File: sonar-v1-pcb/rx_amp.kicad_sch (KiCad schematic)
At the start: 13 parts, among them U301 Opamp_Dual

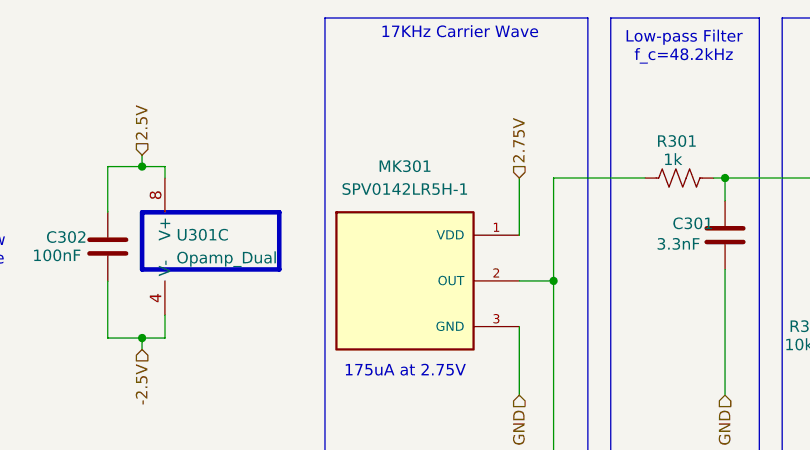
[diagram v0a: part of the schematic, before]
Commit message: Fix pinout
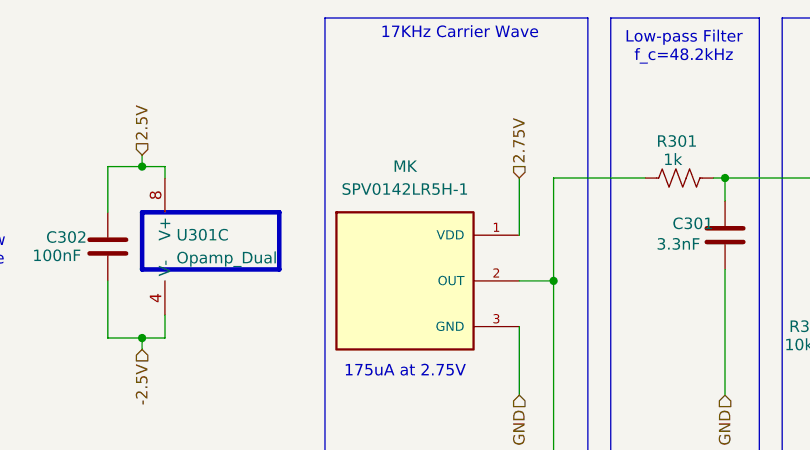
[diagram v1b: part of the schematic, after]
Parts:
- renumbered MK301 to MK

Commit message: Fix the annoattion thing
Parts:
- renumbered MK to MK301
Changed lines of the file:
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@@
 	)
 	(rectangle
-		(start 71.12 80.01)
-		(end 86.36 86.36)
-		(stroke
-			(width 0.508)
-			(type default)
-			(color 255 0 255 1)
-		)
-		(fill
-			(type none)
-		)
-	)
-	(rectangle
 		(start 142.24 58.42)
 		(end 179.07 113.03)
@@
 		)
 	)
-	(rectangle
-		(start 190.5 64.77)
-		(end 205.74 71.12)
-		(stroke
-			(width 0.508)
-			(type default)
-			(color 255 0 255 1)
-		)
-		(fill
-			(type none)
-		)
-	)
-	(rectangle
-		(start 147.32 66.04)
-		(end 162.56 72.39)
-		(stroke
-			(width 0.508)
-			(type default)
-			(color 255 0 255 1)
-		)
-		(fill
-			(type none)
-		)
-	)
 	(text "175uA at 2.75V"
 		(exclude_from_sim no)
@@
 		(dnp no)
 		(fields_autoplaced yes)
-		(property "Reference" "MK"
+		(property "Reference" "MK301"
 			(at 100.33 74.93 0)
 			(effects
@@
 				)
 				(path "/f72ceae0-eee4-4385-b0e8-639846bcb5f2/293969c4-9575-41aa-bb6a-e94ffb52e407/4baae0c7-5504-4fa5-b170-826798e08abe"
-					(reference "MK2102")
+					(reference "MK2101")
 					(unit 1)
 				)
@@
 					(unit 1)
 				)
+				(path "/f72ceae0-eee4-4385-b0e8-639846bcb5f2/d78844ef-eb5d-4b24-a5c3-8824db20c2bc/1e9737bb-54d3-46c6-89c7-bafd5d01cb9f"
+					(reference "MK2601")
+					(unit 1)
+				)
+				(path "/f72ceae0-eee4-4385-b0e8-639846bcb5f2/d78844ef-eb5d-4b24-a5c3-8824db20c2bc/4b88e5a9-a1a4-4236-ac8a-a515268f9e7e"
+					(reference "MK701")
+					(unit 1)
+				)
+				(path "/f72ceae0-eee4-4385-b0e8-639846bcb5f2/d78844ef-eb5d-4b24-a5c3-8824db20c2bc/4baae0c7-5504-4fa5-b170-826798e08abe"
+					(reference "MK301")
+					(unit 1)
+				)
+				(path "/f72ceae0-eee4-4385-b0e8-639846bcb5f2/d78844ef-eb5d-4b24-a5c3-8824db20c2bc/5fa345fd-8f82-4102-b4da-88393397ee2f"
+					(reference "MK1801")
+					(unit 1)
+				)
+				(path "/f72ceae0-eee4-4385-b0e8-639846bcb5f2/d78844ef-eb5d-4b24-a5c3-8824db20c2bc/92589eb0-14ab-438f-abf4-d7e391dbea95"
+					(reference "MK601")
+					(unit 1)
+				)
+				(path "/f72ceae0-eee4-4385-b0e8-639846bcb5f2/d78844ef-eb5d-4b24-a5c3-8824db20c2bc/a69a1e19-7333-49c9-8cfe-abe95e31b9e6"
+					(reference "MK1401")
+					(unit 1)
+				)
+				(path "/f72ceae0-eee4-4385-b0e8-639846bcb5f2/d78844ef-eb5d-4b24-a5c3-8824db20c2bc/da58af52-59a2-42c6-b6e7-fabe3f18277b"
+					(reference "MK1001")
+					(unit 1)
+				)
+				(path "/f72ceae0-eee4-4385-b0e8-639846bcb5f2/d78844ef-eb5d-4b24-a5c3-8824db20c2bc/ef24f3d1-799c-40c0-a32b-fd2185333268"
+					(reference "MK2201")
+					(unit 1)
+				)
 			)
 		)
@@
 				)
 				(path "/f72ceae0-eee4-4385-b0e8-639846bcb5f2/293969c4-9575-41aa-bb6a-e94ffb52e407/5fa345fd-8f82-4102-b4da-88393397ee2f"
-					(reference "U2502")
+					(reference "U2501")
 					(unit 1)
 				)
 				(path "/f72ceae0-eee4-4385-b0e8-639846bcb5f2/293969c4-9575-41aa-bb6a-e94ffb52e407/92589eb0-14ab-438f-abf4-d7e391dbea95"
-					(reference "U2002")
+					(reference "U2001")
 					(unit 1)
 				)
@@
 				)
 				(path "/f72ceae0-eee4-4385-b0e8-639846bcb5f2/d3b8d639-c387-46bd-9010-317ff5495a13/5fa345fd-8f82-4102-b4da-88393397ee2f"
-					(reference "U1303")
+					(reference "U1301")
 					(unit 1)
 				)
 				(path "/f72ceae0-eee4-4385-b0e8-639846bcb5f2/d3b8d639-c387-46bd-9010-317ff5495a13/92589eb0-14ab-438f-abf4-d7e391dbea95"
-					(reference "U802")
+					(reference "U801")
 					(unit 1)
 				)
@@
 			(project "sonar"
 				(path "/f72ceae0-eee4-4385-b0e8-639846bcb5f2/293969c4-9575-41aa-bb6a-e94ffb52e407/1e9737bb-54d3-46c6-89c7-bafd5d01cb9f"
-					(reference "U2502")
+					(reference "U2701")
 					(unit 3)
 				)
@@
 				)
 				(path "/f72ceae0-eee4-4385-b0e8-639846bcb5f2/293969c4-9575-41aa-bb6a-e94ffb52e407/da58af52-59a2-42c6-b6e7-fabe3f18277b"
-					(reference "U2002")
+					(reference "U2301")
 					(unit 3)
 				)
@@
 				)
 				(path "/f72ceae0-eee4-4385-b0e8-639846bcb5f2/d3b8d639-c387-46bd-9010-317ff5495a13/1e9737bb-54d3-46c6-89c7-bafd5d01cb9f"
-					(reference "U1303")
+					(reference "U1501")
 					(unit 3)
 				)
@@
 				)
 				(path "/f72ceae0-eee4-4385-b0e8-639846bcb5f2/d3b8d639-c387-46bd-9010-317ff5495a13/5fa345fd-8f82-4102-b4da-88393397ee2f"
-					(reference "U1302")
+					(reference "U1301")
 					(unit 3)
 				)
@@
 				)
 				(path "/f72ceae0-eee4-4385-b0e8-639846bcb5f2/d3b8d639-c387-46bd-9010-317ff5495a13/a69a1e19-7333-49c9-8cfe-abe95e31b9e6"
-					(reference "U503")
+					(reference "U501")
 					(unit 3)
 				)
 				(path "/f72ceae0-eee4-4385-b0e8-639846bcb5f2/d3b8d639-c387-46bd-9010-317ff5495a13/da58af52-59a2-42c6-b6e7-fabe3f18277b"
-					(reference "U802")
+					(reference "U1101")
 					(unit 3)
 				)
@@
 				)
 				(path "/f72ceae0-eee4-4385-b0e8-639846bcb5f2/d78844ef-eb5d-4b24-a5c3-8824db20c2bc/1e9737bb-54d3-46c6-89c7-bafd5d01cb9f"
-					(reference "U1801")
+					(reference "U2601")
 					(unit 3)
 				)
 				(path "/f72ceae0-eee4-4385-b0e8-639846bcb5f2/d78844ef-eb5d-4b24-a5c3-8824db20c2bc/4b88e5a9-a1a4-4236-ac8a-a515268f9e7e"
-					(reference "U502")
+					(reference "U701")
 					(unit 3)
 				)
@@
 				)
 				(path "/f72ceae0-eee4-4385-b0e8-639846bcb5f2/d78844ef-eb5d-4b24-a5c3-8824db20c2bc/5fa345fd-8f82-4102-b4da-88393397ee2f"
-					(reference "U1101")
+					(reference "U1801")
 					(unit 3)
 				)
 				(path "/f72ceae0-eee4-4385-b0e8-639846bcb5f2/d78844ef-eb5d-4b24-a5c3-8824db20c2bc/92589eb0-14ab-438f-abf4-d7e391dbea95"
-					(reference "U501")
+					(reference "U601")
 					(unit 3)
 				)
 				(path "/f72ceae0-eee4-4385-b0e8-639846bcb5f2/d78844ef-eb5d-4b24-a5c3-8824db20c2bc/a69a1e19-7333-49c9-8cfe-abe95e31b9e6"
-					(reference "U803")
+					(reference "U1401")
 					(unit 3)
 				)
 				(path "/f72ceae0-eee4-4385-b0e8-639846bcb5f2/d78844ef-eb5d-4b24-a5c3-8824db20c2bc/da58af52-59a2-42c6-b6e7-fabe3f18277b"
-					(reference "U601")
+					(reference "U1001")
 					(unit 3)
 				)
 				(path "/f72ceae0-eee4-4385-b0e8-639846bcb5f2/d78844ef-eb5d-4b24-a5c3-8824db20c2bc/ef24f3d1-799c-40c0-a32b-fd2185333268"
-					(reference "U1301")
+					(reference "U2201")
 					(unit 3)
 				)
@@
 			(project "sonar"
 				(path "/f72ceae0-eee4-4385-b0e8-639846bcb5f2/293969c4-9575-41aa-bb6a-e94ffb52e407/1e9737bb-54d3-46c6-89c7-bafd5d01cb9f"
-					(reference "U2502")
+					(reference "U2701")
 					(unit 2)
 				)
@@
 				)
 				(path "/f72ceae0-eee4-4385-b0e8-639846bcb5f2/293969c4-9575-41aa-bb6a-e94ffb52e407/da58af52-59a2-42c6-b6e7-fabe3f18277b"
-					(reference "U2002")
+					(reference "U2301")
 					(unit 2)
 				)
@@
 				)
 				(path "/f72ceae0-eee4-4385-b0e8-639846bcb5f2/d3b8d639-c387-46bd-9010-317ff5495a13/1e9737bb-54d3-46c6-89c7-bafd5d01cb9f"
-					(reference "U1303")
+					(reference "U1501")
 					(unit 2)
 				)
@@
 				)
 				(path "/f72ceae0-eee4-4385-b0e8-639846bcb5f2/d3b8d639-c387-46bd-9010-317ff5495a13/5fa345fd-8f82-4102-b4da-88393397ee2f"
-					(reference "U1302")
+					(reference "U1301")
 					(unit 2)
 				)
@@
 				)
 				(path "/f72ceae0-eee4-4385-b0e8-639846bcb5f2/d3b8d639-c387-46bd-9010-317ff5495a13/a69a1e19-7333-49c9-8cfe-abe95e31b9e6"
-					(reference "U503")
+					(reference "U501")
 					(unit 2)
 				)
 				(path "/f72ceae0-eee4-4385-b0e8-639846bcb5f2/d3b8d639-c387-46bd-9010-317ff5495a13/da58af52-59a2-42c6-b6e7-fabe3f18277b"
-					(reference "U802")
+					(reference "U1101")
 					(unit 2)
 				)
@@
 				)
 				(path "/f72ceae0-eee4-4385-b0e8-639846bcb5f2/d78844ef-eb5d-4b24-a5c3-8824db20c2bc/1e9737bb-54d3-46c6-89c7-bafd5d01cb9f"
-					(reference "U1801")
+					(reference "U2601")
 					(unit 2)
 				)
 				(path "/f72ceae0-eee4-4385-b0e8-639846bcb5f2/d78844ef-eb5d-4b24-a5c3-8824db20c2bc/4b88e5a9-a1a4-4236-ac8a-a515268f9e7e"
-					(reference "U502")
+					(reference "U701")
 					(unit 2)
 				)
@@
 				)
 				(path "/f72ceae0-eee4-4385-b0e8-639846bcb5f2/d78844ef-eb5d-4b24-a5c3-8824db20c2bc/5fa345fd-8f82-4102-b4da-88393397ee2f"
-					(reference "U1101")
+					(reference "U1801")
 					(unit 2)
 				)
 				(path "/f72ceae0-eee4-4385-b0e8-639846bcb5f2/d78844ef-eb5d-4b24-a5c3-8824db20c2bc/92589eb0-14ab-438f-abf4-d7e391dbea95"
-					(reference "U501")
+					(reference "U601")
 					(unit 2)
 				)
 				(path "/f72ceae0-eee4-4385-b0e8-639846bcb5f2/d78844ef-eb5d-4b24-a5c3-8824db20c2bc/a69a1e19-7333-49c9-8cfe-abe95e31b9e6"
-					(reference "U803")
+					(reference "U1401")
 					(unit 2)
 				)
 				(path "/f72ceae0-eee4-4385-b0e8-639846bcb5f2/d78844ef-eb5d-4b24-a5c3-8824db20c2bc/da58af52-59a2-42c6-b6e7-fabe3f18277b"
-					(reference "U601")
+					(reference "U1001")
 					(unit 2)
 				)
 				(path "/f72ceae0-eee4-4385-b0e8-639846bcb5f2/d78844ef-eb5d-4b24-a5c3-8824db20c2bc/ef24f3d1-799c-40c0-a32b-fd2185333268"
-					(reference "U1301")
+					(reference "U2201")
 					(unit 2)
 				)

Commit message: formatting lol
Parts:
- TP301: value TestPoint_Probe -> AMP_TO_ADC
- TP302: value TestPoint_Probe -> PRE_AMP_OUT
- TP303: value TestPoint_Probe -> MIC_SIGNAL
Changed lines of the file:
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@@
 			)
 		)
-		(property "Value" "TestPoint_Probe"
+		(property "Value" "MIC_SIGNAL"
 			(at 113.284 108.204 0)
 			(effects
@@
 		(dnp no)
 		(property "Reference" "R305"
-			(at 143.002 92.71 0)
+			(at 141.224 92.456 0)
 			(effects
 				(font
@@
 			)
 		)
-		(property "Value" "TestPoint_Probe"
+		(property "Value" "PRE_AMP_OUT"
 			(at 163.576 70.358 0)
 			(effects
@@
 		(dnp no)
 		(property "Reference" "C301"
-			(at 130.048 81.28 0)
+			(at 127.254 81.28 0)
 			(effects
 				(font
@@
 			)
 		)
-		(property "Value" "TestPoint_Probe"
+		(property "Value" "AMP_TO_ADC"
 			(at 222.25 70.8024 0)
 			(effects

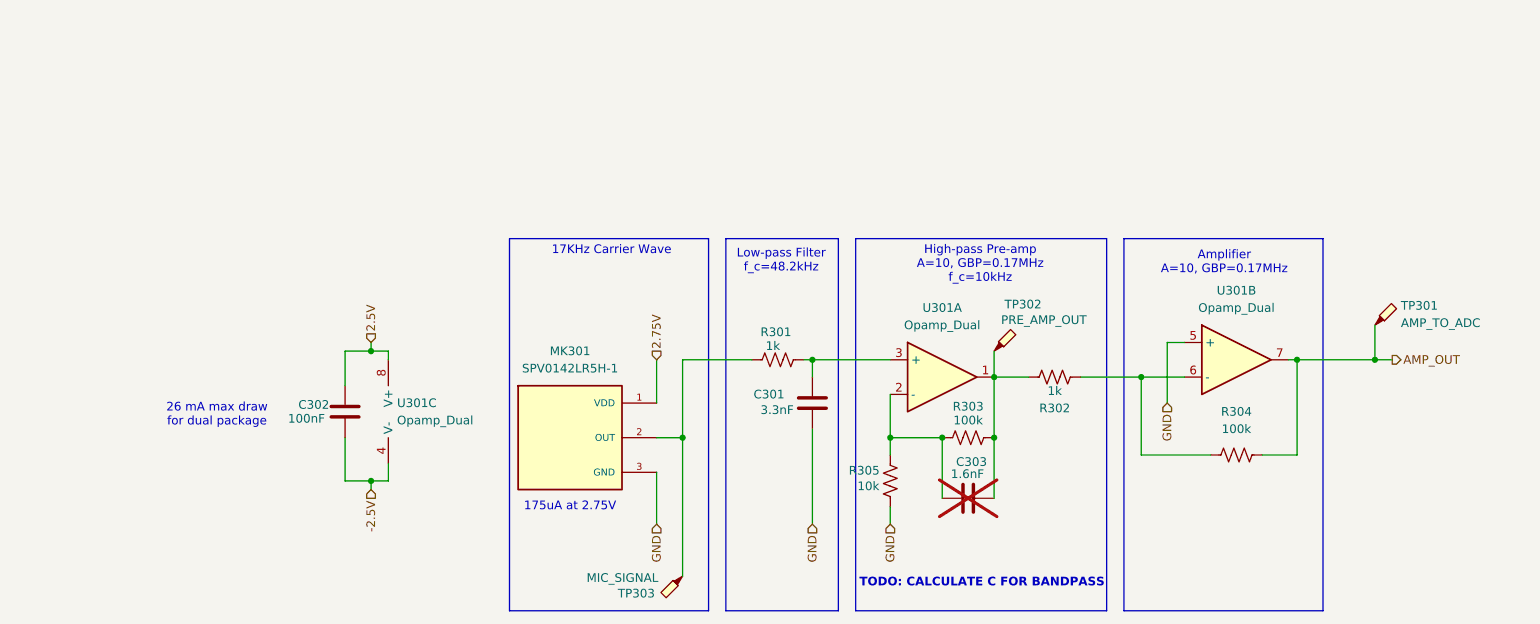
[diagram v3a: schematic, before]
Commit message: Update inverting buck boost schematic
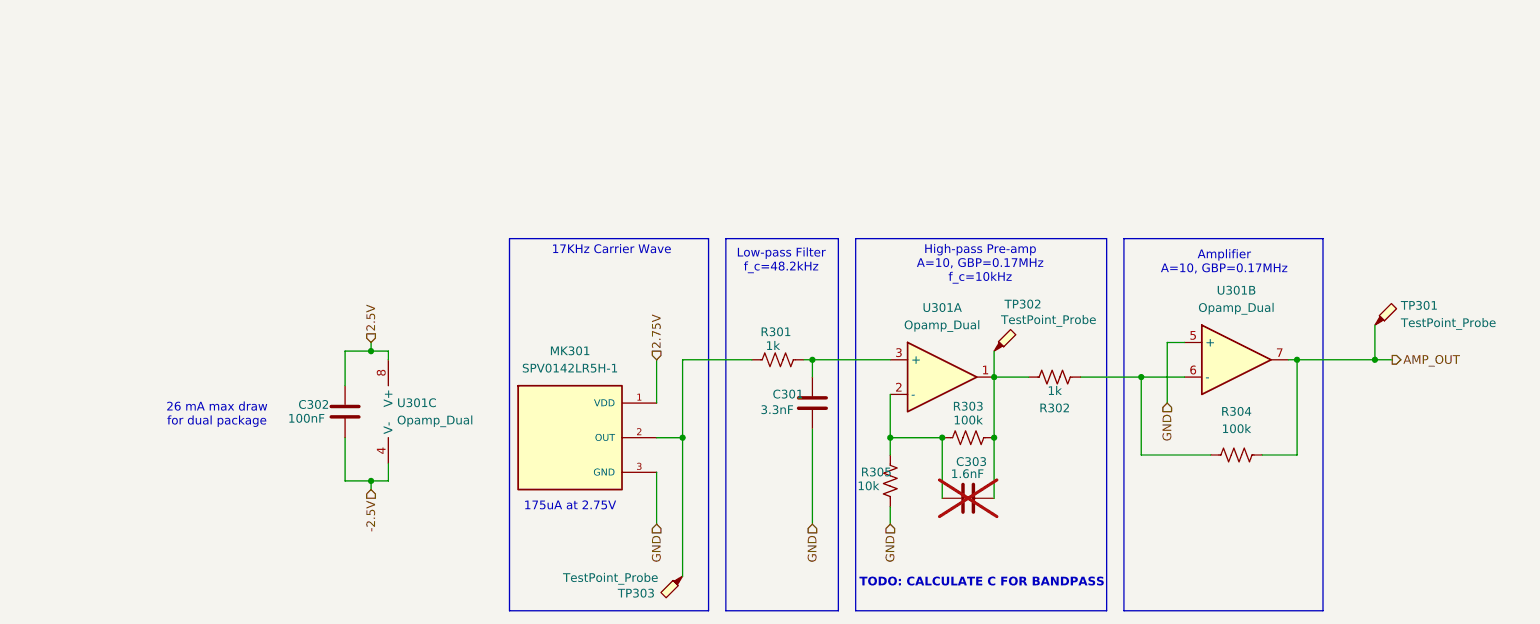
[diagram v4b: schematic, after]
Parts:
- TP301: value AMP_TO_ADC -> TestPoint_Probe
- TP302: value PRE_AMP_OUT -> TestPoint_Probe
- TP303: value MIC_SIGNAL -> TestPoint_Probe
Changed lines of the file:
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@@
 			)
 		)
-		(property "Value" "MIC_SIGNAL"
+		(property "Value" "TestPoint_Probe"
 			(at 113.284 108.204 0)
 			(effects
@@
 		(dnp no)
 		(property "Reference" "R305"
-			(at 141.224 92.456 0)
+			(at 143.002 92.71 0)
 			(effects
 				(font
@@
 			)
 		)
-		(property "Value" "PRE_AMP_OUT"
+		(property "Value" "TestPoint_Probe"
 			(at 163.576 70.358 0)
 			(effects
@@
 		(dnp no)
 		(property "Reference" "C301"
-			(at 127.254 81.28 0)
+			(at 130.048 81.28 0)
 			(effects
 				(font
@@
 			)
 		)
-		(property "Value" "AMP_TO_ADC"
+		(property "Value" "TestPoint_Probe"
 			(at 222.25 70.8024 0)
 			(effects

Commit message: Make some small visual edits
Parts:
- removed C303: 1.6nF, Capacitor_SMD:C_0402_1005Metric, symbol Device:C
- removed R301, R302: 1k, Resistor_SMD:R_0402_1005Metric, symbol Device:R_US
- removed R303, R304: 100k, Resistor_SMD:R_0402_1005Metric, symbol Device:R_US
- removed R305: 10k, Resistor_SMD:R_0402_1005Metric, symbol Device:R_US
- added C7: 1.6nF, GS_Capacitors:C_0603_1608Metric, symbol GS_Capacitor_0603:C_0603_1.6nF
- added R3, R6: 1k, GS_Resistors:R_0603_1608Metric, symbol GS_Resistor_0603:R_0603_1k
- added R4: 10k, GS_Resistors:R_0603_1608Metric, symbol GS_Resistor_0603:R_0603_10k
- added R5, R7: 100k, GS_Resistors:R_0603_1608Metric, symbol GS_Resistor_0603:R_0603_100k
- TP3: renamed from TP303; value TestPoint_Probe -> RX.RAW
- TP4: renamed from TP302; value TestPoint_Probe -> RX.PRE
- TP5: renamed from TP301; value TestPoint_Probe -> RX.AMP
- renumbered C302 to C5, C301 to C6, MK301 to MK1, U301 to U2
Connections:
- net -2.5V is gone; now on net GND: C5.2, U2.4 (V-)
- net AMP_OUT: now also R7.2
- net GND: now also R4.2
- net at C6.1, U2.3 (+): now also R3.2
- net at MK1.2 (OUT), TP3.1: now also R3.1
- net at U2.6 (-): now also R6.2, R7.1
- net at TP4.1, U2.1: now also C7.2, R5.2, R6.1
- net at U2.2 (-): now also C7.1, R4.1, R5.1
- net 2.5V renamed 3.3V
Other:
- title: (none) -> Microphone and Amplification Stage
- moved on the sheet: C5, C6, MK1, TP3, TP4, TP5, U2A, U2B, U2C
